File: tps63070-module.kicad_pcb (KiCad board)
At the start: 2 copper layers, 16.8 x 22.1 mm, 23 parts, among them J1 Conn_01x02_Male, J2 Conn_01x02_Male, J3 Conn_01x03_Male, J4 Conn_01x01_Male, J5 Conn_01x02_Male, J6 Conn_01x02_Male, U1 tps63070

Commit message: Do some routing
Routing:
- net /PS: track 0.00 -> 7.79 mm
- net /VSEL: track 0.00 -> 5.33 mm, vias 0 -> 1
- net /EN: track 0.00 -> 4.34 mm
- net Net-(L1-Pad2): vias 0 -> 7
- net Net-(L1-Pad1): vias 0 -> 7
- added copper zone on F.Cu, net /VIN
- added copper zone on F.Cu, net /VOUT
- added copper zone on F.Cu, net GND
- added copper zone on B.Cu, net Net-(L1-Pad1)
- added copper zone on B.Cu, net Net-(L1-Pad2)
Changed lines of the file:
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@@
     (thickness 1.6)
     (drawings 4)
-    (tracks 0)
+    (tracks 29)
     (zones 0)
     (modules 23)
@@
     (user_trace_width 1)
     (trace_clearance 0.127)
-    (zone_clearance 0.508)
+    (zone_clearance 0.127)
     (zone_45_only no)
     (trace_min 0.127)
@@
   (gr_line (start 20.07 42.41) (end 36.83 42.41) (layer Edge.Cuts) (width 0.05))
   (gr_line (start 20.07 20.31) (end 20.07 42.41) (layer Edge.Cuts) (width 0.05))
+  (via (at 30.984 32.24) (size 0.6) (drill 0.3) (layers F.Cu B.Cu) (net 5))
+  (segment (start 30.439 31.81) (end 30.554 31.81) (width 0.127) (layer F.Cu) (net 5))
+  (segment (start 30.554 31.81) (end 30.984 32.24) (width 0.127) (layer F.Cu) (net 5))
+  (segment (start 28.476 34.323736) (end 28.476 34.357919) (width 0.127) (layer B.Cu) (net 5))
+  (segment (start 28.476 34.357919) (end 28.476 35.56) (width 0.127) (layer B.Cu) (net 5))
+  (segment (start 30.559736 32.24) (end 28.476 34.323736) (width 0.127) (layer B.Cu) (net 5))
+  (segment (start 30.984 32.24) (end 30.559736 32.24) (width 0.127) (layer B.Cu) (net 5))
+  (segment (start 29.939 33.89) (end 29.939 31.81) (width 0.127) (layer F.Cu) (net 6))
+  (segment (start 31.539 35.49) (end 29.939 33.89) (width 0.127) (layer F.Cu) (net 6))
+  (segment (start 32.30451 37.54949) (end 32.30451 34.66051) (width 0.127) (layer F.Cu) (net 7))
+  (segment (start 31.539 37.64) (end 32.214 37.64) (width 0.127) (layer F.Cu) (net 7))
+  (segment (start 32.214 37.64) (end 32.30451 37.54949) (width 0.127) (layer F.Cu) (net 7))
+  (segment (start 32.30451 34.66051) (end 31.984 34.34) (width 0.127) (layer F.Cu) (net 7))
+  (segment (start 31.984 32.28) (end 30.864 31.16) (width 0.127) (layer F.Cu) (net 7))
+  (segment (start 31.984 34.34) (end 31.984 32.28) (width 0.127) (layer F.Cu) (net 7))
+  (via (at 23.284 31.44) (size 0.6) (drill 0.3) (layers F.Cu B.Cu) (net 10))
+  (via (at 23.984 31.44) (size 0.6) (drill 0.3) (layers F.Cu B.Cu) (net 10))
+  (via (at 24.684 31.44) (size 0.6) (drill 0.3) (layers F.Cu B.Cu) (net 10))
+  (via (at 25.384 31.44) (size 0.6) (drill 0.3) (layers F.Cu B.Cu) (net 10))
+  (via (at 23.284 29.44) (size 0.6) (drill 0.3) (layers F.Cu B.Cu) (net 9))
+  (via (at 23.984 29.44) (size 0.6) (drill 0.3) (layers F.Cu B.Cu) (net 9))
+  (via (at 24.684 29.44) (size 0.6) (drill 0.3) (layers F.Cu B.Cu) (net 9))
+  (via (at 25.384 29.44) (size 0.6) (drill 0.3) (layers F.Cu B.Cu) (net 9))
+  (via (at 28.884 29.8) (size 0.6) (drill 0.3) (layers F.Cu B.Cu) (net 9))
+  (via (at 28.274 29.8) (size 0.6) (drill 0.3) (layers F.Cu B.Cu) (net 9))
+  (via (at 29.494 29.8) (size 0.6) (drill 0.3) (layers F.Cu B.Cu) (net 9))
+  (via (at 28.274 31.02) (size 0.6) (drill 0.3) (layers F.Cu B.Cu) (net 10))
+  (via (at 28.884 31.02) (size 0.6) (drill 0.3) (layers F.Cu B.Cu) (net 10))
+  (via (at 29.494 31.02) (size 0.6) (drill 0.3) (layers F.Cu B.Cu) (net 10))
+  (zone (net 9) (net_name "Net-(L1-Pad2)") (layer B.Cu) (hatch edge 0.508)
+    (priority 50)
+    (connect_pads yes (clearance 0.127))
+    (min_thickness 0.127)
+    (fill yes (arc_segments 32) (thermal_gap 0.508) (thermal_bridge_width 0.508))
+    (polygon
+      (pts
+        (xy 22.134 28.64) (xy 25.834 28.64) (xy 28.084 29.59) (xy 29.784 29.59) (xy 29.784 30.14)
+        (xy 28.084 30.14) (xy 25.834 29.89) (xy 22.134 29.89)
+      )
+    )
+  )
+  (zone (net 10) (net_name "Net-(L1-Pad1)") (layer B.Cu) (hatch edge 0.508)
+    (priority 50)
+    (connect_pads yes (clearance 0.127))
+    (min_thickness 0.127)
+    (fill yes (arc_segments 32) (thermal_gap 0.508) (thermal_bridge_width 0.508))
+    (polygon
+      (pts
+        (xy 22.134 32.19) (xy 25.834 32.19) (xy 28.084 31.24) (xy 29.784 31.24) (xy 29.784 30.69)
+        (xy 28.084 30.69) (xy 25.834 30.94) (xy 22.134 30.94)
+      )
+    )
+  )
+  (zone (net 1) (net_name GND) (layer F.Cu) (hatch edge 0.508)
+    (priority 50)
+    (connect_pads yes (clearance 0.127))
+    (min_thickness 0.127)
+    (fill yes (arc_segments 32) (thermal_gap 0.508) (thermal_bridge_width 0.508))
+    (polygon
+      (pts
+        (xy 26.584 28.84) (xy 27.784 28.84) (xy 27.784 29.94) (xy 28.084 30.14) (xy 30.084 30.14)
+        (xy 30.084 30.64) (xy 28.084 30.64) (xy 27.784 30.94) (xy 27.784 32.04) (xy 26.584 32.04)
+      )
+    )
+  )
+  (zone (net 4) (net_name /VOUT) (layer F.Cu) (hatch edge 0.508)
+    (priority 25)
+    (connect_pads yes (clearance 0.127))
+    (min_thickness 0.127)
+    (fill yes (arc_segments 32) (thermal_gap 0.508) (thermal_bridge_width 0.508))
+    (polygon
+      (pts
+        (xy 29.684 29.44) (xy 29.684 24.34) (xy 28.184 24.34) (xy 27.484 25.74) (xy 26.084 26.24)
+        (xy 24.784 26.24) (xy 24.784 27.84) (xy 26.684 28.44) (xy 27.784 28.44) (xy 28.684 29.44)
+      )
+    )
+  )
+  (zone (net 2) (net_name /VIN) (layer F.Cu) (hatch edge 0.508)
+    (priority 25)
+    (connect_pads yes (clearance 0.127))
+    (min_thickness 0.127)
+    (fill yes (arc_segments 32) (thermal_gap 0.508) (thermal_bridge_width 0.508))
+    (polygon
+      (pts
+        (xy 29.684 31.44) (xy 29.684 34.34) (xy 28.284 34.34) (xy 26.084 34.64) (xy 24.684 34.64)
+        (xy 24.684 32.94) (xy 26.084 32.94) (xy 26.784 32.44) (xy 27.784 32.44) (xy 28.784 31.44)
+      )
+    )
+  )
 )

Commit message: Add groundplanes
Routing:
- added copper zone on B.Cu, net GND
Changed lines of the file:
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@@
     (connect_pads yes (clearance 0.127))
     (min_thickness 0.127)
-    (fill yes (arc_segments 32) (thermal_gap 0.508) (thermal_bridge_width 0.508))
+    (fill (arc_segments 32) (thermal_gap 0.508) (thermal_bridge_width 0.508))
     (polygon
       (pts
@@
     (connect_pads yes (clearance 0.127))
     (min_thickness 0.127)
-    (fill yes (arc_segments 32) (thermal_gap 0.508) (thermal_bridge_width 0.508))
+    (fill (arc_segments 32) (thermal_gap 0.508) (thermal_bridge_width 0.508))
     (polygon
       (pts
@@
     (connect_pads yes (clearance 0.127))
     (min_thickness 0.127)
-    (fill yes (arc_segments 32) (thermal_gap 0.508) (thermal_bridge_width 0.508))
+    (fill (arc_segments 32) (thermal_gap 0.508) (thermal_bridge_width 0.508))
     (polygon
       (pts
@@
     (connect_pads yes (clearance 0.127))
     (min_thickness 0.127)
-    (fill yes (arc_segments 32) (thermal_gap 0.508) (thermal_bridge_width 0.508))
+    (fill (arc_segments 32) (thermal_gap 0.508) (thermal_bridge_width 0.508))
     (polygon
       (pts
@@
     (connect_pads yes (clearance 0.127))
     (min_thickness 0.127)
-    (fill yes (arc_segments 32) (thermal_gap 0.508) (thermal_bridge_width 0.508))
+    (fill (arc_segments 32) (thermal_gap 0.508) (thermal_bridge_width 0.508))
     (polygon
       (pts
@@
       )
     )
+  )
+  (zone (net 1) (net_name GND) (layer F.Cu) (hatch edge 0.508)
+    (connect_pads yes (clearance 0.127))
+    (min_thickness 0.127)
+    (fill (arc_segments 32) (thermal_gap 0.508) (thermal_bridge_width 0.508))
+    (polygon
+      (pts
+        (xy 20.084 20.34) (xy 36.784 20.34) (xy 36.784 42.34) (xy 20.084 42.34)
+      )
+    )
+  )
+  (zone (net 1) (net_name GND) (layer B.Cu) (hatch edge 0.508)
+    (connect_pads yes (clearance 0.127))
+    (min_thickness 0.127)
+    (fill (arc_segments 32) (thermal_gap 0.508) (thermal_bridge_width 0.508))
+    (polygon
+      (pts
+        (xy 20.084 20.34) (xy 36.784 20.34) (xy 36.784 42.34) (xy 20.084 42.34)
+      )
+    )

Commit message: Route board
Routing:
- net /VOUT: track 0.00 -> 20.7 mm
- net Net-(J4-Pad1): track 0.00 -> 14.1 mm, vias 0 -> 1
- net /VIN: track 0.00 -> 13.7 mm, vias 0 -> 13
- net /FB: track 0.00 -> 11.3 mm
- net Net-(R4-Pad2): track 0.00 -> 8.00 mm
- net /PS: track 7.79 -> 12.1 mm
- net /EN: track 4.34 -> 8.49 mm
- net /VSEL: track 5.33 -> 9.28 mm
- net Net-(C5-Pad2): track 0.00 -> 2.59 mm
- net GND: vias 0 -> 13
- added copper zone on B.Cu, net /VIN

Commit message: Add PCB art
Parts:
- added G***: LOGO, tps63070:catboy, B.Cu at (29.2, 28.5)
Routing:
- net /VIN: track 13.7 -> 18.5 mm
- net GND: vias 13 -> 16
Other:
- board text added: "EN"
- board text added: "GND"
- board text added: "PGOOD"
- board text added: "PS"
- board text added: "VIN"
- board text added: "VOUT"
- board text added: "VSEL"

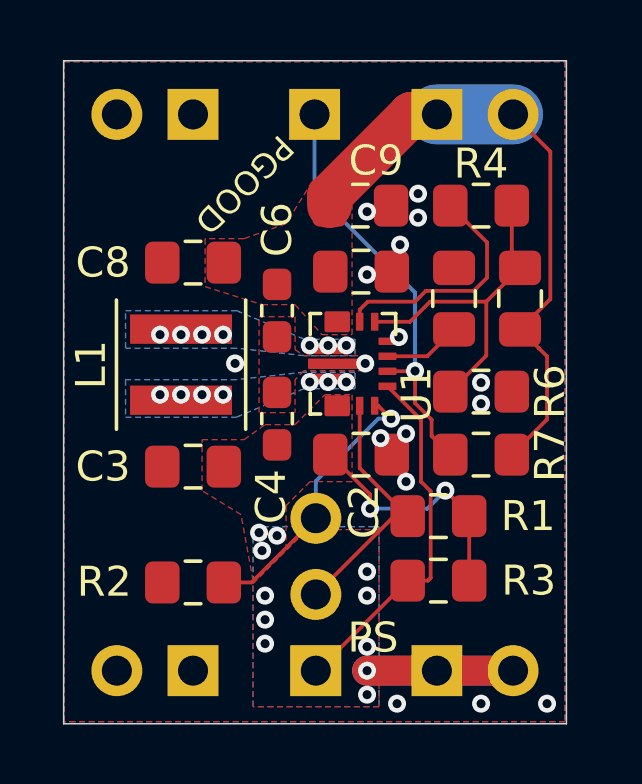
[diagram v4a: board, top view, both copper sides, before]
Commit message: Connect VOUT on top Cu layer, too
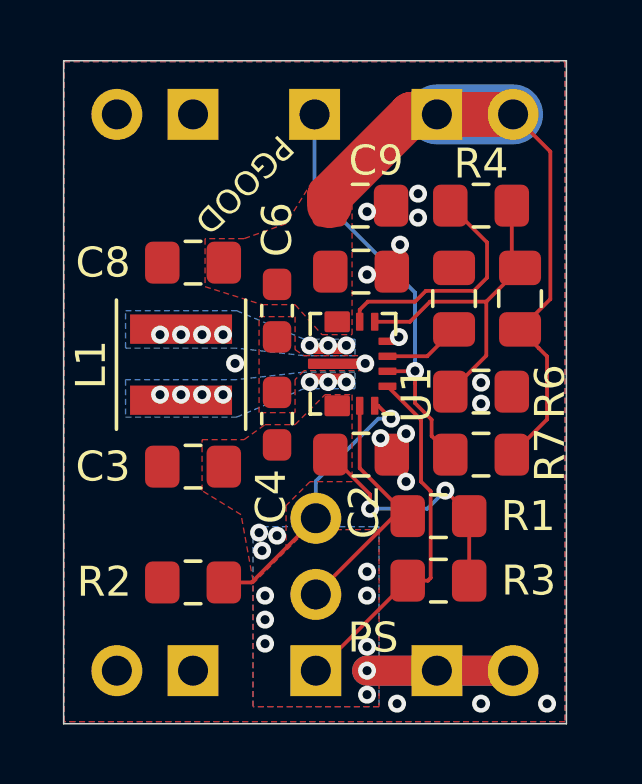
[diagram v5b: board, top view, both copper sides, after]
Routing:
- net /VOUT: track 20.7 -> 23.2 mm
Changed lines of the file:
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@@
     (thickness 1.6)
     (drawings 12)
-    (tracks 117)
+    (tracks 118)
     (zones 0)
     (modules 24)
@@
   )
   (setup
-    (last_trace_width 1)
+    (last_trace_width 1.5)
     (user_trace_width 0.127)
     (user_trace_width 0.25)
@@
   (segment (start 31.657166 22.098) (end 32.512 22.098) (width 1.5) (layer F.Cu) (net 4))
   (segment (start 28.934 25.14) (end 28.934 24.821166) (width 1.5) (layer F.Cu) (net 4))
+  (segment (start 35.052 22.098) (end 32.512 22.098) (width 1.5) (layer F.Cu) (net 4))
   (via (at 30.984 32.24) (size 0.6) (drill 0.3) (layers F.Cu B.Cu) (net 5))
   (segment (start 30.439 31.81) (end 30.554 31.81) (width 0.127) (layer F.Cu) (net 5))

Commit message: Add more silkscreen designators
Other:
- board text added: "2019"
- board text added: "Rev A"
- board text added: "Schramm"
- board text added: "Tobias"
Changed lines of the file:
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@@
   (general
     (thickness 1.6)
-    (drawings 12)
+    (drawings 16)
     (tracks 118)
     (zones 0)
@@
     )
   )
+  (gr_text 2019 (at 22.684 35.74) (layer F.SilkS)
+    (effects (font (size 1 1) (thickness 0.15)))
+  )
+  (gr_text "Rev A" (at 22.784 24.14) (layer F.SilkS)
+    (effects (font (size 1 1) (thickness 0.15)))
+  )
+  (gr_text Schramm (at 22.484 31.44 90) (layer B.SilkS)
+    (effects (font (size 1 1) (thickness 0.15)) (justify mirror))
+  )
+  (gr_text Tobias (at 20.984 30.44 90) (layer B.SilkS)
+    (effects (font (size 1 1) (thickness 0.15)) (justify mirror))
+  )
   (gr_text VSEL (at 24.884 35.64) (layer B.SilkS)

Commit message: Add 3d models
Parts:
- L1: footprint Inductor_SMD:L_Coilcraft_XxL4020 -> tps63070:L_Coilcraft_XxL4020

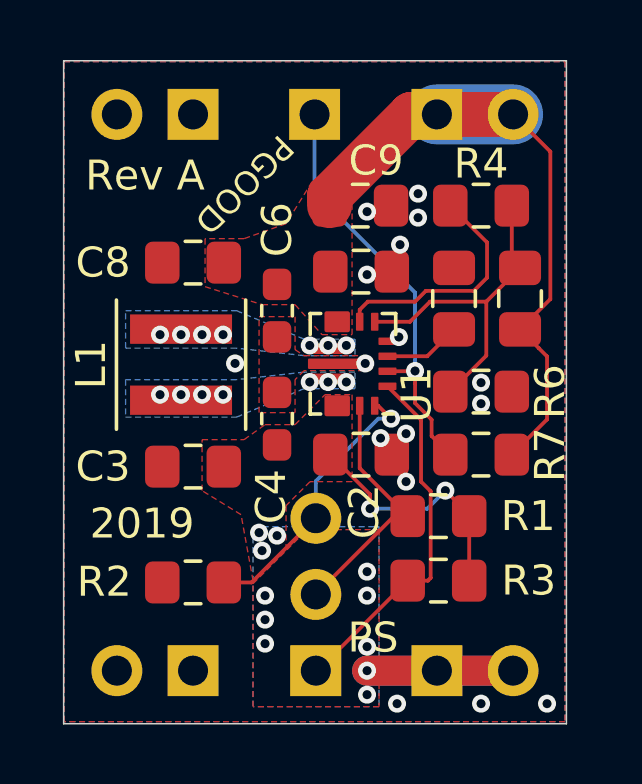
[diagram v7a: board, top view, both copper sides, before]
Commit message: Add module footprints and 3d models
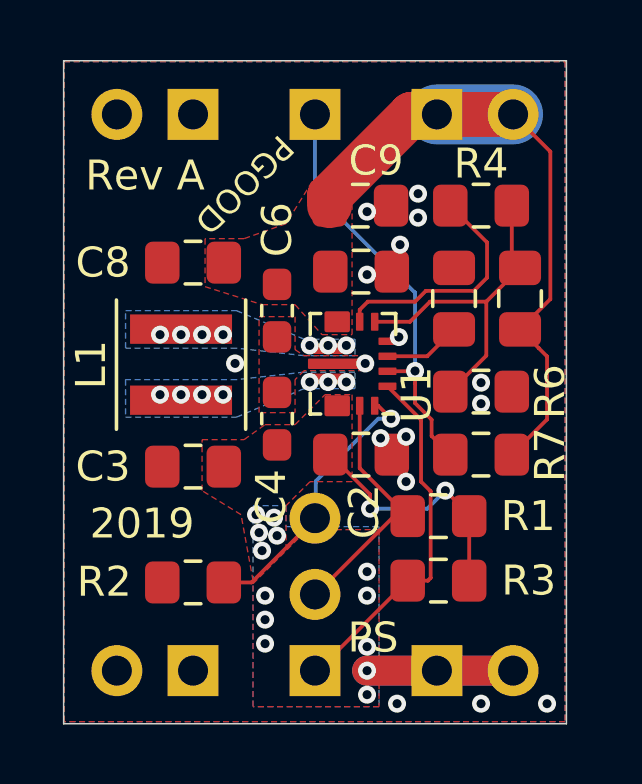
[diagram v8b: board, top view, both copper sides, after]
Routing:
- net /VIN: vias 13 -> 15
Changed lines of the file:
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@@
     (thickness 1.6)
     (drawings 16)
-    (tracks 118)
+    (tracks 121)
     (zones 0)
     (modules 24)
@@
   )
   (module Connector_PinHeader_2.54mm:PinHeader_1x01_P2.54mm_Vertical (layer B.Cu)
-    (at 28.435 22.098)
+    (at 28.447 22.098)
     (descr "Through hole straight pin header, 1x01, 2.54mm pitch, single row")
     (tags "Through hole pin header THT 1x01 2.54mm single row")
@@
   )
   (module Connector_PinHeader_2.54mm:PinHeader_1x03_P2.54mm_Vertical (layer B.Cu)
-    (at 28.476 40.64)
+    (at 28.447 40.639)
     (descr "Through hole straight pin header, 1x03, 2.54mm pitch, single row")
     (tags "Through hole pin header THT 1x03 2.54mm single row")
@@
   (via (at 30.124 30.4) (size 0.6) (drill 0.3) (layers F.Cu B.Cu) (net 1))
   (via (at 31.484 34.34) (size 0.6) (drill 0.3) (layers F.Cu B.Cu) (net 1))
-  (via (at 31.484 32.74) (size 0.6) (drill 0.3) (layers F.Cu B.Cu) (net 1))
+  (via (at 31.484 32.84) (size 0.6) (drill 0.3) (layers F.Cu B.Cu) (net 1))
   (via (at 31.184 41.74) (size 0.6) (drill 0.3) (layers F.Cu B.Cu) (net 1))
   (via (at 36.184 41.74) (size 0.6) (drill 0.3) (layers F.Cu B.Cu) (net 1))
@@
   (segment (start 35.052 40.64) (end 32.512 40.64) (width 1) (layer F.Cu) (net 2))
   (segment (start 32.512 40.64) (end 30.184 40.64) (width 1) (layer F.Cu) (net 2))
+  (via (at 26.484 35.44) (size 0.6) (drill 0.3) (layers F.Cu B.Cu) (net 2))
+  (via (at 27.084 35.54) (size 0.6) (drill 0.3) (layers F.Cu B.Cu) (net 2))
   (segment (start 32.189 30.16) (end 33.084 29.265) (width 0.127) (layer F.Cu) (net 3))
   (segment (start 30.864 30.16) (end 32.189 30.16) (width 0.127) (layer F.Cu) (net 3))
@@
   (segment (start 31.984 32.28) (end 30.864 31.16) (width 0.127) (layer F.Cu) (net 7))
   (segment (start 31.984 34.34) (end 31.984 32.28) (width 0.127) (layer F.Cu) (net 7))
-  (segment (start 28.539 40.64) (end 28.476 40.64) (width 0.127) (layer F.Cu) (net 7))
-  (segment (start 31.539 37.64) (end 28.539 40.64) (width 0.127) (layer F.Cu) (net 7))
+  (segment (start 28.54 40.639) (end 28.447 40.639) (width 0.127) (layer F.Cu) (net 7))
+  (segment (start 31.539 37.64) (end 28.54 40.639) (width 0.127) (layer F.Cu) (net 7))
   (segment (start 31.7745 30.66) (end 31.784 30.6505) (width 0.127) (layer F.Cu) (net 8))
   (via (at 31.784 30.6505) (size 0.6) (drill 0.3) (layers F.Cu B.Cu) (net 8))
   (segment (start 30.864 30.66) (end 31.7745 30.66) (width 0.127) (layer F.Cu) (net 8))
-  (segment (start 28.435 24.691) (end 28.435 22.098) (width 0.127) (layer B.Cu) (net 8))
   (segment (start 31.784 30.6505) (end 31.784 28.04) (width 0.127) (layer B.Cu) (net 8))
-  (segment (start 31.784 28.04) (end 28.435 24.691) (width 0.127) (layer B.Cu) (net 8))
   (segment (start 31.784 31.720776) (end 31.784 31.074764) (width 0.127) (layer F.Cu) (net 8))
   (segment (start 32.335628 32.272404) (end 31.784 31.720776) (width 0.127) (layer F.Cu) (net 8))
@@
   (segment (start 31.784 31.074764) (end 31.784 30.6505) (width 0.127) (layer F.Cu) (net 8))
   (segment (start 32.959 33.44) (end 32.335628 32.816628) (width 0.127) (layer F.Cu) (net 8))
+  (segment (start 28.447 22.098) (end 28.447 24.705) (width 0.127) (layer B.Cu) (net 8))
+  (segment (start 31.782 28.04) (end 31.784 28.04) (width 0.127) (layer B.Cu) (net 8))
+  (segment (start 28.447 24.705) (end 31.782 28.04) (width 0.127) (layer B.Cu) (net 8))
   (via (at 23.284 29.44) (size 0.6) (drill 0.3) (layers F.Cu B.Cu) (net 9))
   (via (at 23.984 29.44) (size 0.6) (drill 0.3) (layers F.Cu B.Cu) (net 9))
@@
     (polygon
       (pts
-        (xy 30.584 41.84) (xy 26.384 41.84) (xy 26.384 35.84) (xy 30.584 35.84)
+        (xy 30.584 41.84) (xy 26.384 41.84) (xy 26.384 35.14) (xy 27.484 35.14) (xy 27.484 35.84)
+        (xy 30.584 35.84)
       )
     )
